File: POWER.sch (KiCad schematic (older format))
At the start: 34 parts, among them U201 TPS61021A, U402 MAX1555

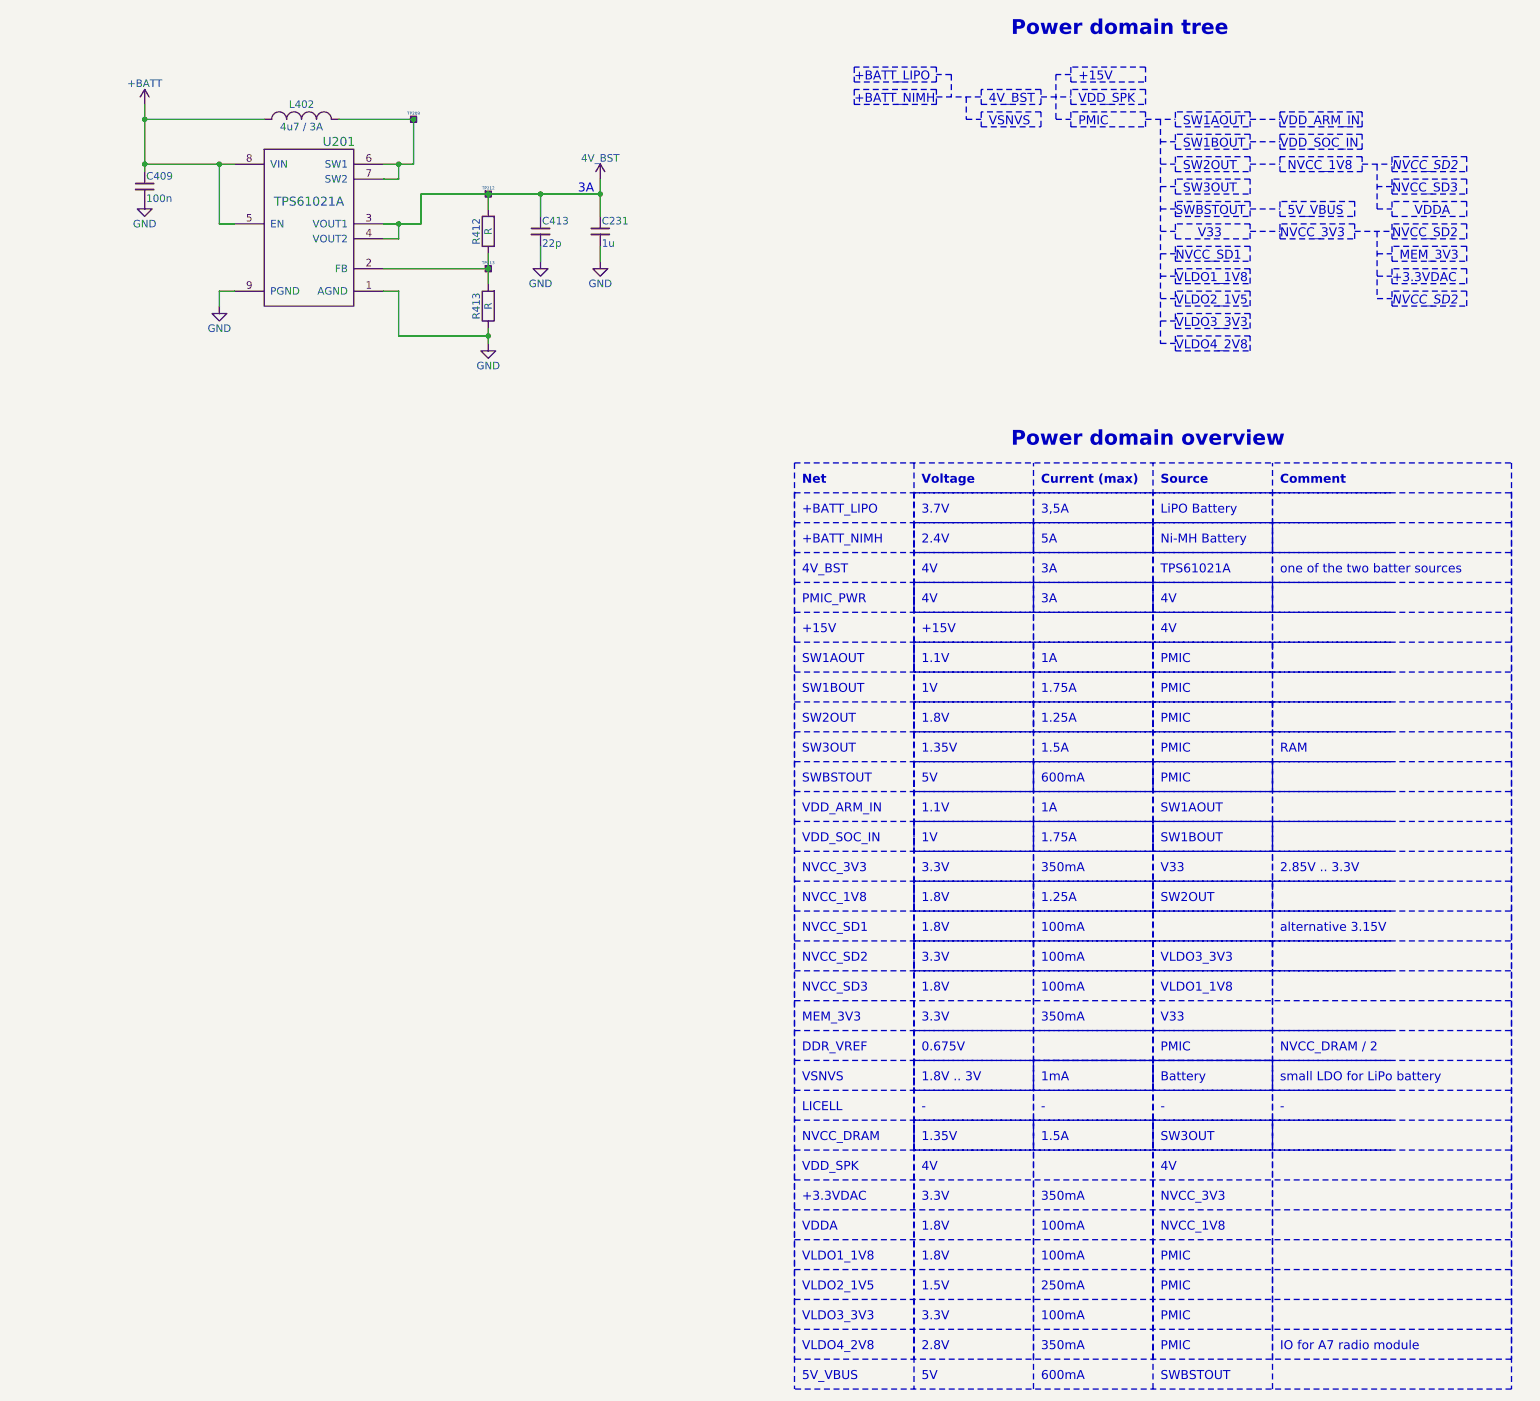
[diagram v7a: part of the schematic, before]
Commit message: Modified power nets Added table of contents
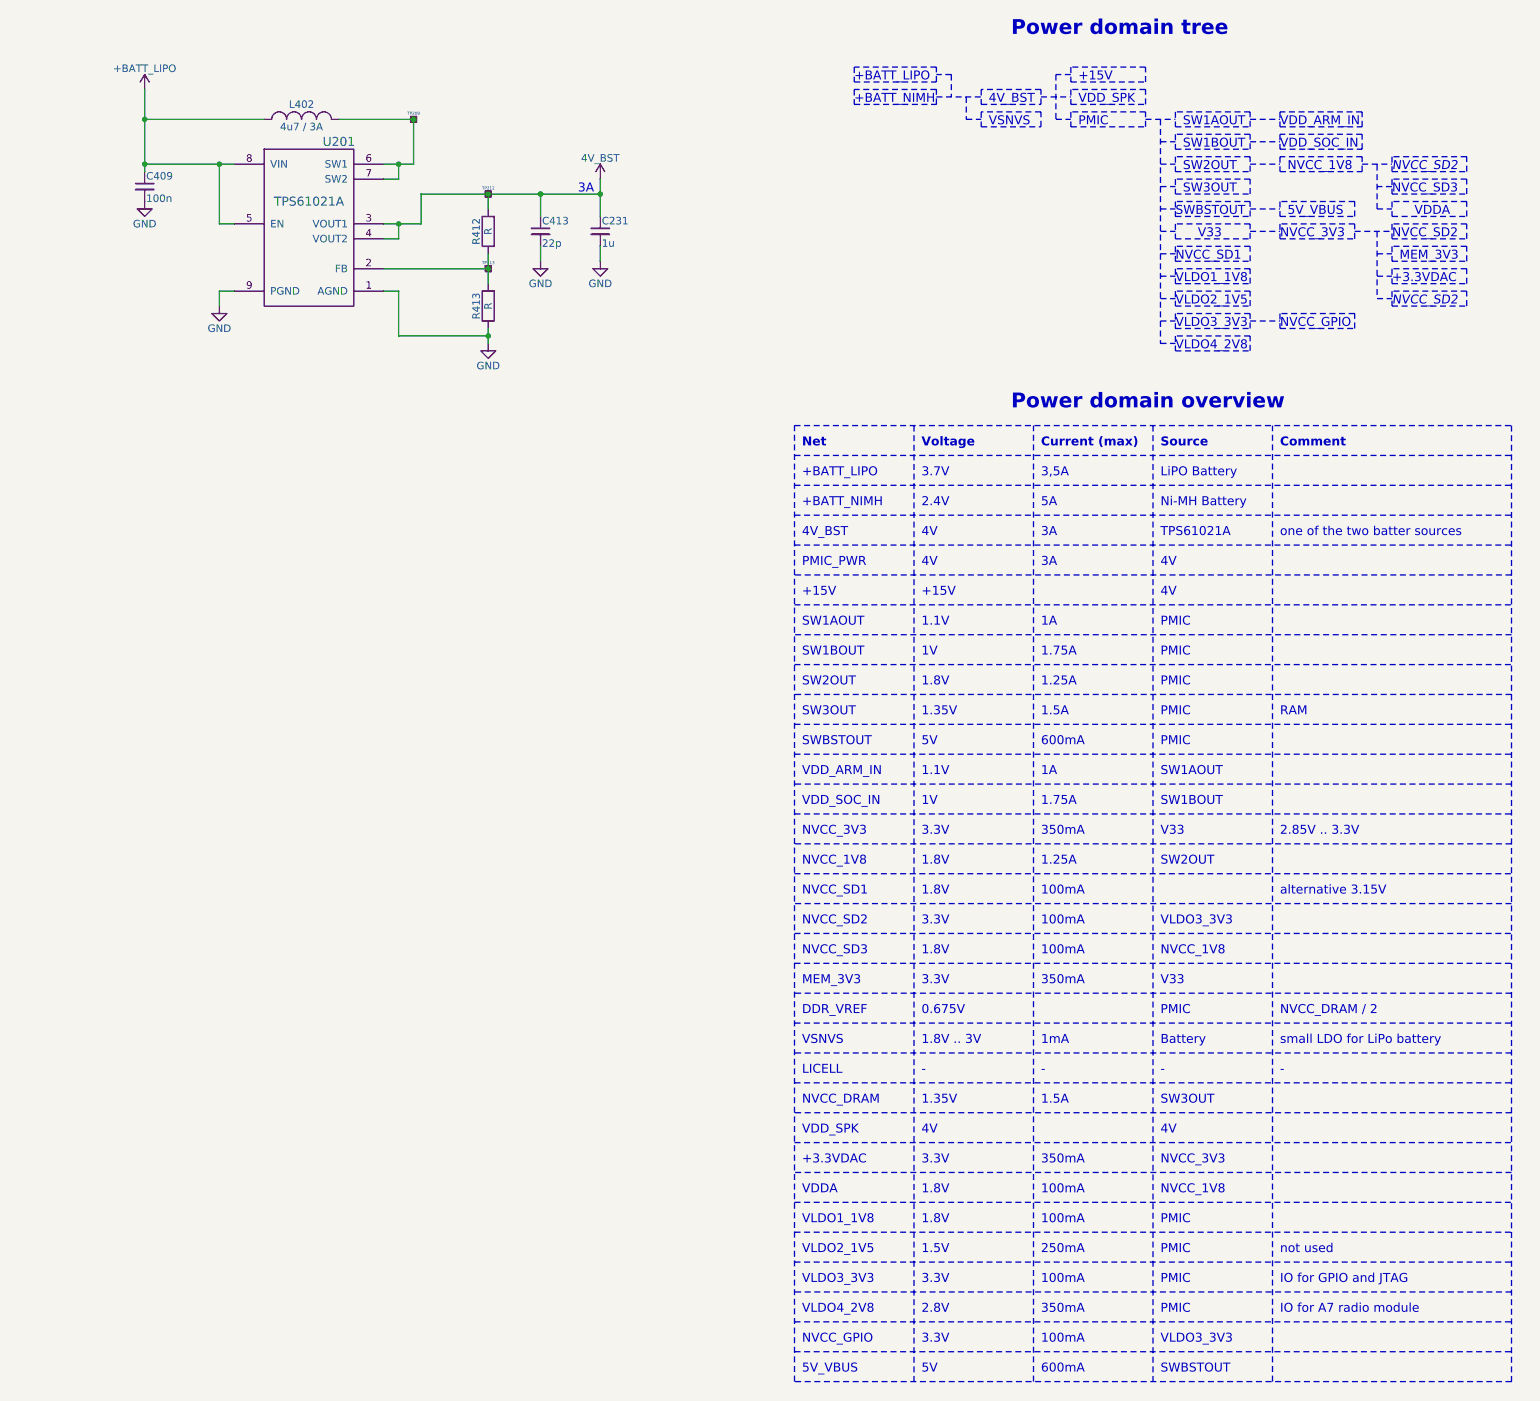
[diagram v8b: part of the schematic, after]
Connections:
- net +BATT is gone; now on net +BATT_LIPO: C409.1, L402.1, U201.5 (EN), U201.8 (VIN)
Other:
- note added: "IO for GPIO and JTAG"
- note added: "NVCC_GPIO"
- note added: "not used"
